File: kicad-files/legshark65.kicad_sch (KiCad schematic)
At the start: 157 parts, among them SW1 K2-1187SQ-A4SW-06, SW2 PCM12SMTR, T2 53261-0471, U1 STM32F411CEU6, U3 AT24C256C-SSHL-T, Y1 TAXM8M4RFDCET2T

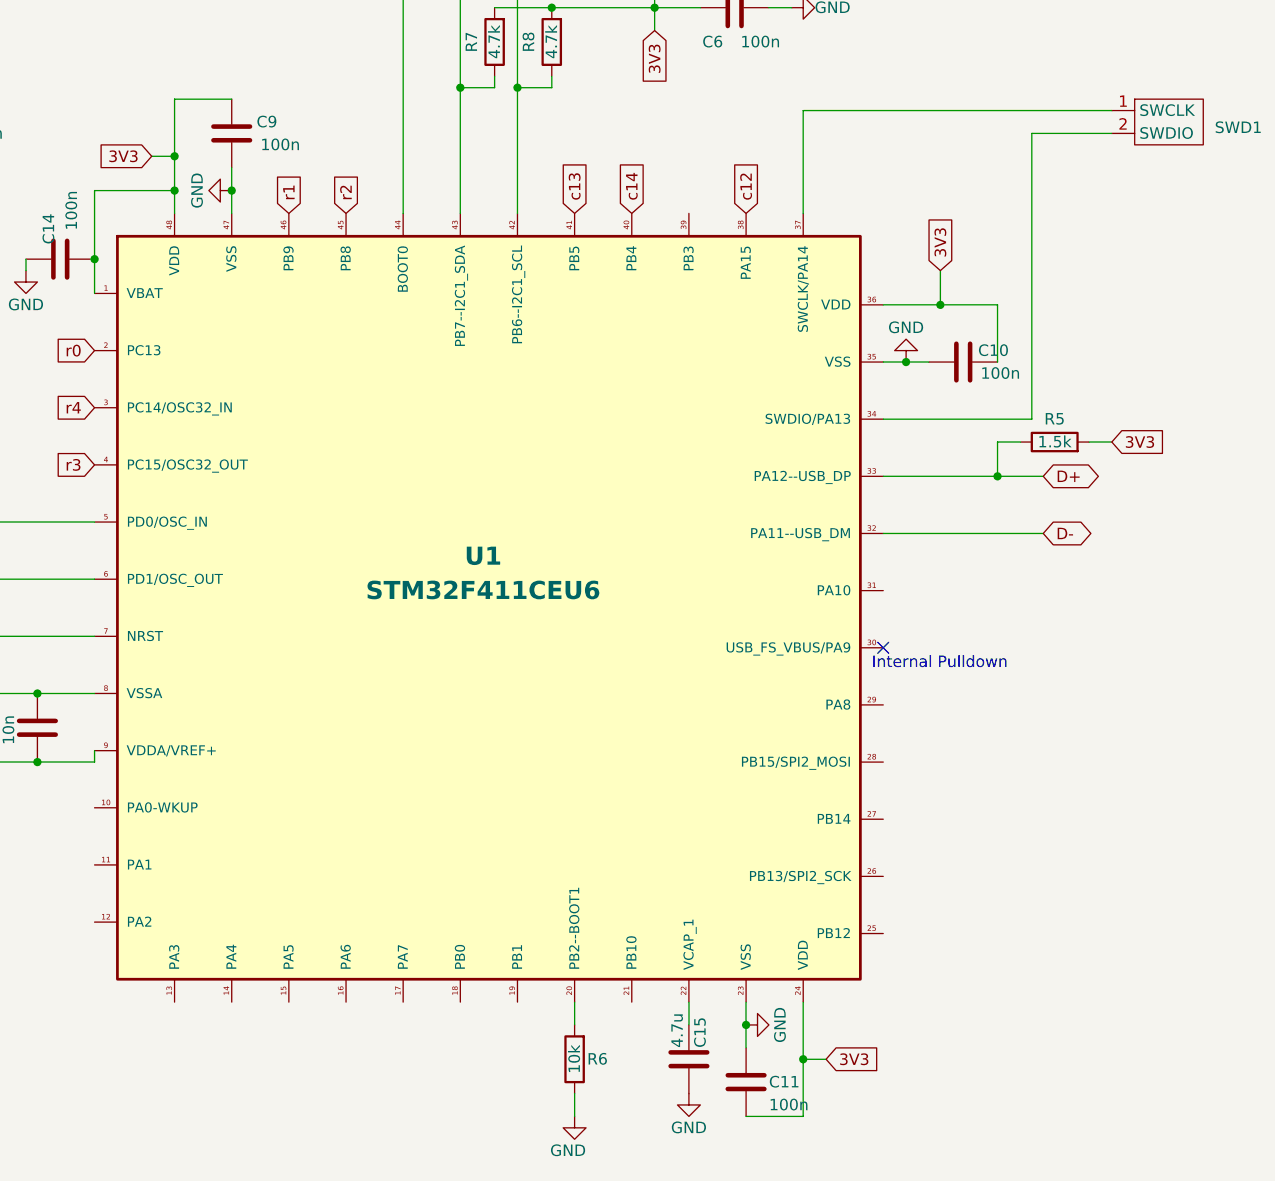
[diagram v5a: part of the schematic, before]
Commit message: Connected all of the wires of the new board
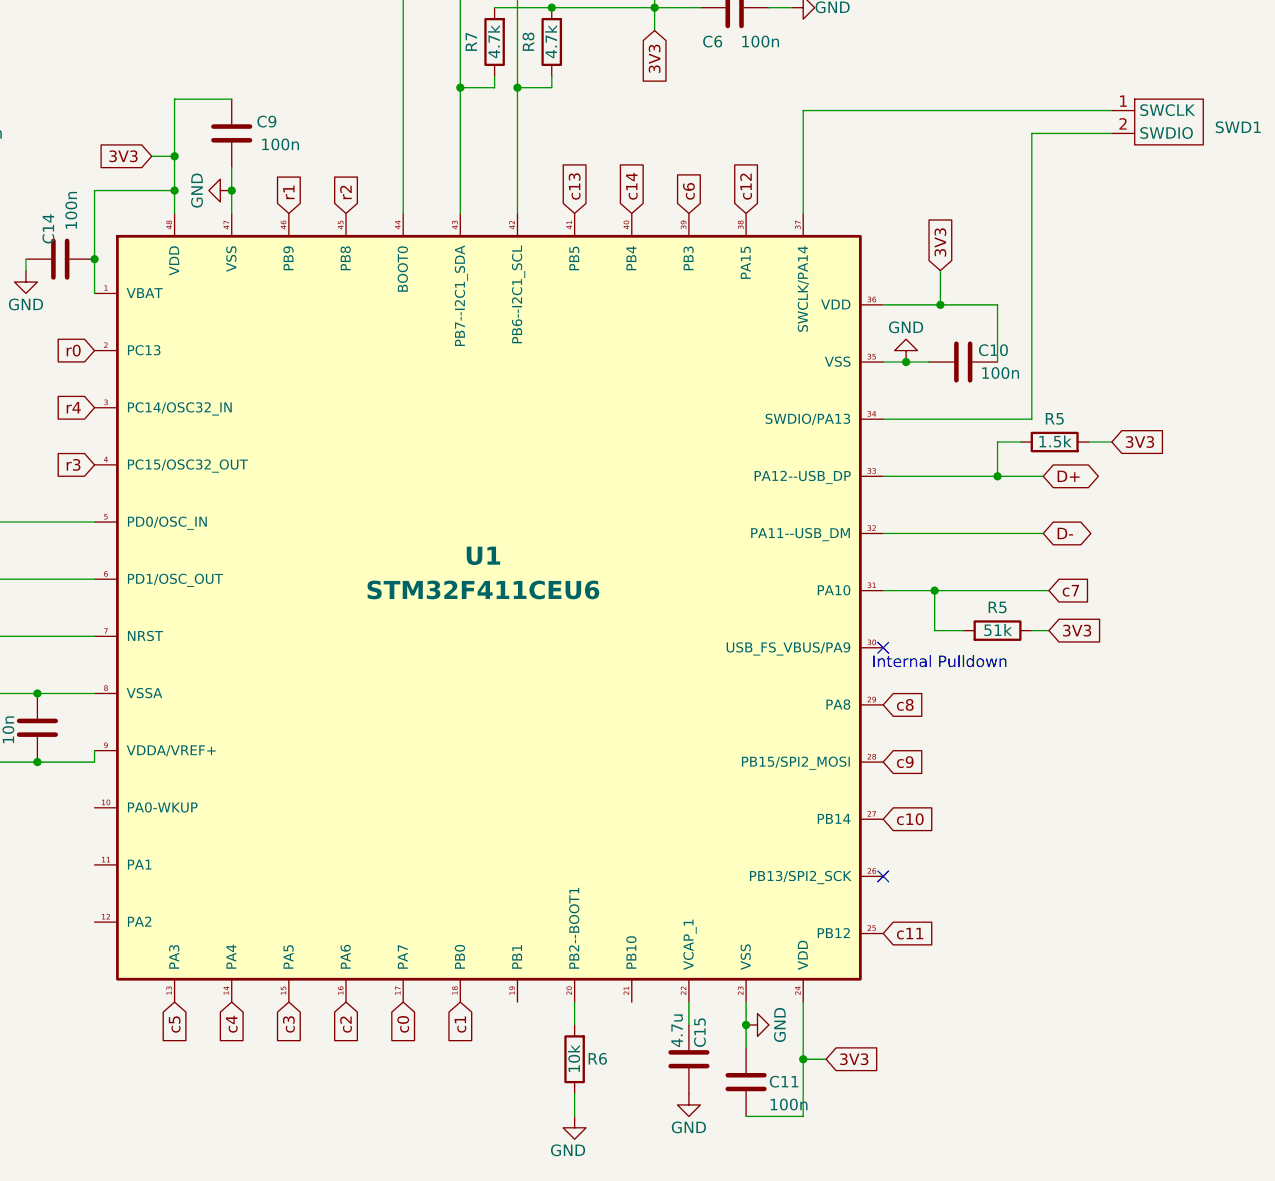
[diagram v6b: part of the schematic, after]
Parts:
- added R5: 51k, Resistor_SMD:R_0603_1608Metric, symbol Device:R
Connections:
- net 3V3: now also R5.1
- net c0: now also U1.17 (PA7)
- net c1: now also U1.18 (PB0)
- net c10: now also U1.27 (PB14)
- net c11: now also U1.25 (PB12)
- net c2: now also U1.16 (PA6)
- net c3: now also U1.15 (PA5)
- net c4: now also U1.14 (PA4)
- net c5: now also U1.13 (PA3)
- net c6: now also U1.39 (PB3)
- net c7: now also U1.31 (PA10), R5.2
- net c8: now also U1.29 (PA8)
- net c9: now also U1.28 (PB15/SPI2_MOSI)
- no-connect marks 1 -> 2
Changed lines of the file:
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@@
   (junction (at 356.235 71.755) (diameter 0) (color 0 0 0 0)
   )
+  (junction (at 220.345 260.35) (diameter 0) (color 0 0 0 0)
+  )
   (junction (at 217.17 234.95) (diameter 0) (color 0 0 0 0)
   )
@@
   )
   (no_connect (at 214.63 266.7))
+  (no_connect (at 214.63 292.1))
   (wire (pts (xy 104.14 203.2) (xy 109.22 203.2))
     (stroke (width 0) (type default))
@@
     (stroke (width 0) (type default))
   )
+  (wire (pts (xy 214.63 260.35) (xy 220.345 260.35))
+    (stroke (width 0) (type default))
+  )
   (wire (pts (xy 381.635 71.755) (xy 407.035 71.755))
     (stroke (width 0) (type default))
@@
     (stroke (width 0) (type default))
   )
+  (wire (pts (xy 220.345 260.35) (xy 233.045 260.35))
+    (stroke (width 0) (type default))
+  )
   (wire (pts (xy 407.035 40.005) (xy 407.035 41.275))
     (stroke (width 0) (type default))
@@
     (stroke (width 0) (type default))
   )
+  (wire (pts (xy 233.045 264.795) (xy 231.14 264.795))
+    (stroke (width 0) (type default))
+  )
   (wire (pts (xy 356.235 90.805) (xy 356.235 92.075))
     (stroke (width 0) (type default))
@@
     (stroke (width 0) (type default))
   )
+  (wire (pts (xy 220.345 264.795) (xy 220.345 260.35))
+    (stroke (width 0) (type default))
+  )
   (wire (pts (xy 120.65 271.78) (xy 127 271.78))
     (stroke (width 0) (type default))
@@
   )
   (wire (pts (xy 113.665 136.525) (xy 113.665 111.125))
+    (stroke (width 0) (type default))
+  )
+  (wire (pts (xy 223.52 264.795) (xy 220.345 264.795))
     (stroke (width 0) (type default))
   )
@@
     )
   )
+  (global_label "c10" (shape input) (at 214.63 285.75 0) (fields_autoplaced)
+    (effects (font (size 1.27 1.27)) (justify left))
+    (property "Intersheetrefs" "${INTERSHEET_REFS}" (at 220.3892 285.75 0)
+      (effects (font (size 1.27 1.27)) (justify left) hide)
+    )
+  )
   (global_label "c0" (shape input) (at 62.865 27.305 180)
     (effects (font (size 1.27 1.27)) (justify right))
@@
     )
   )
+  (global_label "c6" (shape input) (at 193.04 218.44 90) (fields_autoplaced)
+    (effects (font (size 1.27 1.27)) (justify left))
+    (property "Intersheetrefs" "${INTERSHEET_REFS}" (at 193.04 213.8903 90)
+      (effects (font (size 1.27 1.27)) (justify left) hide)
+    )
+  )
+  (global_label "c3" (shape input) (at 148.59 306.07 270) (fields_autoplaced)
+    (effects (font (size 1.27 1.27)) (justify right))
+    (property "Intersheetrefs" "${INTERSHEET_REFS}" (at 148.59 310.6197 90)
+      (effects (font (size 1.27 1.27)) (justify right) hide)
+    )
+  )
   (global_label "r1" (shape input) (at 148.59 218.44 90) (fields_autoplaced)
     (effects (font (size 1.27 1.27)) (justify left))
@@
     )
   )
+  (global_label "3V3" (shape input) (at 233.045 264.795 0) (fields_autoplaced)
+    (effects (font (size 1.27 1.27)) (justify left))
+    (property "Intersheetrefs" "${INTERSHEET_REFS}" (at 238.8042 264.795 0)
+      (effects (font (size 1.27 1.27)) (justify left) hide)
+    )
+  )
   (global_label "c11" (shape input) (at 342.265 27.305 180)
     (effects (font (size 1.27 1.27)) (justify right))
@@
     )
   )
+  (global_label "c4" (shape input) (at 142.24 306.07 270) (fields_autoplaced)
+    (effects (font (size 1.27 1.27)) (justify right))
+    (property "Intersheetrefs" "${INTERSHEET_REFS}" (at 142.24 310.6197 90)
+      (effects (font (size 1.27 1.27)) (justify right) hide)
+    )
+  )
   (global_label "c4" (shape input) (at 164.465 27.305 180)
     (effects (font (size 1.27 1.27)) (justify right))
@@
     )
   )
+  (global_label "c0" (shape input) (at 161.29 306.07 270) (fields_autoplaced)
+    (effects (font (size 1.27 1.27)) (justify right))
+    (property "Intersheetrefs" "${INTERSHEET_REFS}" (at 161.29 310.6197 90)
+      (effects (font (size 1.27 1.27)) (justify right) hide)
+    )
+  )
   (global_label "c5" (shape input) (at 189.865 27.305 180)
     (effects (font (size 1.27 1.27)) (justify right))
@@
     (effects (font (size 1.27 1.27)) (justify right))
     (property "Intersheetrefs" "${INTERSHEET_REFS}" (at 127.5908 212.09 0)
+      (effects (font (size 1.27 1.27)) (justify right) hide)
+    )
+  )
+  (global_label "c2" (shape input) (at 154.94 306.07 270) (fields_autoplaced)
+    (effects (font (size 1.27 1.27)) (justify right))
+    (property "Intersheetrefs" "${INTERSHEET_REFS}" (at 154.94 310.6197 90)
       (effects (font (size 1.27 1.27)) (justify right) hide)
     )
@@
     )
   )
+  (global_label "c5" (shape input) (at 135.89 306.07 270) (fields_autoplaced)
+    (effects (font (size 1.27 1.27)) (justify right))
+    (property "Intersheetrefs" "${INTERSHEET_REFS}" (at 135.89 310.6197 90)
+      (effects (font (size 1.27 1.27)) (justify right) hide)
+    )
+  )
+  (global_label "c7" (shape input) (at 233.045 260.35 0) (fields_autoplaced)
+    (effects (font (size 1.27 1.27)) (justify left))
+    (property "Intersheetrefs" "${INTERSHEET_REFS}" (at 237.5947 260.35 0)
+      (effects (font (size 1.27 1.27)) (justify left) hide)
+    )
+  )
+  (global_label "c8" (shape input) (at 214.63 273.05 0) (fields_autoplaced)
+    (effects (font (size 1.27 1.27)) (justify left))
+    (property "Intersheetrefs" "${INTERSHEET_REFS}" (at 219.1797 273.05 0)
+      (effects (font (size 1.27 1.27)) (justify left) hide)
+    )
+  )
+  (global_label "c11" (shape input) (at 214.63 298.45 0) (fields_autoplaced)
+    (effects (font (size 1.27 1.27)) (justify left))
+    (property "Intersheetrefs" "${INTERSHEET_REFS}" (at 220.3892 298.45 0)
+      (effects (font (size 1.27 1.27)) (justify left) hide)
+    )
+  )
   (global_label "3V3" (shape input) (at 99.06 279.4 180) (fields_autoplaced)
     (effects (font (size 1.27 1.27)) (justify right))
     (property "Intersheetrefs" "${INTERSHEET_REFS}" (at 93.3008 279.4 0)
       (effects (font (size 1.27 1.27)) (justify right) hide)
+    )
+  )
+  (global_label "c9" (shape input) (at 214.63 279.4 0) (fields_autoplaced)
+    (effects (font (size 1.27 1.27)) (justify left))
+    (property "Intersheetrefs" "${INTERSHEET_REFS}" (at 219.1797 279.4 0)
+      (effects (font (size 1.27 1.27)) (justify left) hide)
     )
   )
@@
     )
   )
+  (global_label "c1" (shape input) (at 167.64 306.07 270) (fields_autoplaced)
+    (effects (font (size 1.27 1.27)) (justify right))
+    (property "Intersheetrefs" "${INTERSHEET_REFS}" (at 167.64 310.6197 90)
+      (effects (font (size 1.27 1.27)) (justify right) hide)
+    )
+  )
   (global_label "r0" (shape input) (at 40.005 46.355 180)
     (effects (font (size 1.27 1.27)) (justify right))
@@
         )
       )
+    )
+  )
+  (symbol (lib_id "Device:R") (at 227.33 264.795 270) (mirror x) (unit 1)
+    (in_bom yes) (on_board yes) (dnp no)
+    (property "Reference" "R5" (at 227.33 262.255 90)
+      (effects (font (size 1.27 1.27)))
+    )
+    (property "Value" "51k" (at 227.33 264.795 90)
+      (effects (font (size 1.27 1.27)))
+    )
+    (property "Footprint" "Resistor_SMD:R_0603_1608Metric" (at 227.33 266.573 90)
+      (effects (font (size 1.27 1.27)) hide)
+    )
+    (property "Datasheet" "~" (at 227.33 264.795 0)
+      (effects (font (size 1.27 1.27)) hide)
+    )
+    (pin "1")
+    (pin "2")
+    (instances
+      (project "old_layout"
+        (path "/2fda2561-53ed-4930-8b41-858e0e3dd5f4"
+          (reference "R5") (unit 1)
+        )
+      )
+      (project "legshark65"
+        (path "/9ddf6dc5-8b5e-413a-9b25-d1d5a5a60469"
+          (reference "R1") (unit 1)
+        )
+      )

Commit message: Lost of small changes to board
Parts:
- D_0, D_1, D_10, D_11, D_12, D_13, D_14, D_15, D_16, D_17, D_18, D_19, D_2, D_20, D_21, D_22, D_23, D_24, D_25, D_26, D_27, D_28, D_29, D_3, D_30, D_31, D_32, D_33, D_34, D_35, D_36, D_37, D_38, D_39, D_4, D_40, D_41, D_42, D_43, D_44, D_45, D_46, D_47, D_48, D_49, D_5, D_50, D_51, D_52, D_53, D_54, D_55, D_56, D_57, D_58, D_59, D_6, D_60, D_61, D_62, D_63, D_64, D_7, D_8, D_9: footprint Diode_SMD:D_SOD-123 -> acheron_Components:D_SOD-123

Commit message: Finished wiring the board
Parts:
- removed SWD1: ~, Legshark:1x02_Long_Header, symbol legshark_symbols:2PinHeader
- added J1: ARM JTAG, acheron_Connectors:PinHeader_2x5_P2.54mm_Vertical, symbol Connector_Generic:Conn_02x05_Odd_Even
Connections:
- net 3V3: now also J1.7 (Pin_7), J1.8 (Pin_8)
- net GND: now also J1.10 (Pin_10), J1.3 (Pin_3), J1.4 (Pin_4)
- net NRST: now reaches C7.2, R11.2, U1.7 (NRST)
- net NRST: now also J1.9 (Pin_9)
- net BOOT1: now reaches R6.2, U1.20 (PB2--BOOT1)
- net BOOT1: now also J1.6 (Pin_6)
- net SWDIO: now reaches U1.34 (SWDIO/PA13)
- net SWDIO: now also J1.1 (Pin_1)
- net SWCLK: now reaches U1.37 (SWCLK/PA14)
- net SWCLK: now also J1.2 (Pin_2)
- net BOOT0: now reaches C17.2, R15.1, U1.44 (BOOT0)
- net BOOT0: now also J1.5 (Pin_5)
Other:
- moved on the sheet: C16, Legshark_Logo2, T2
